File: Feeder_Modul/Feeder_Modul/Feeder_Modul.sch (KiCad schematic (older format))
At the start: 101 parts, among them J1 Conn_02x01, J101 Conn_02x01, J102 Conn_01x06_Male, J103 Conn_02x01, J104 Conn_02x01, J105 Conn_02x01, J106 WE_629104190121, J107 Conn_02x07_Odd_Even, J108 Conn_02x01, J109 Conn_02x01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

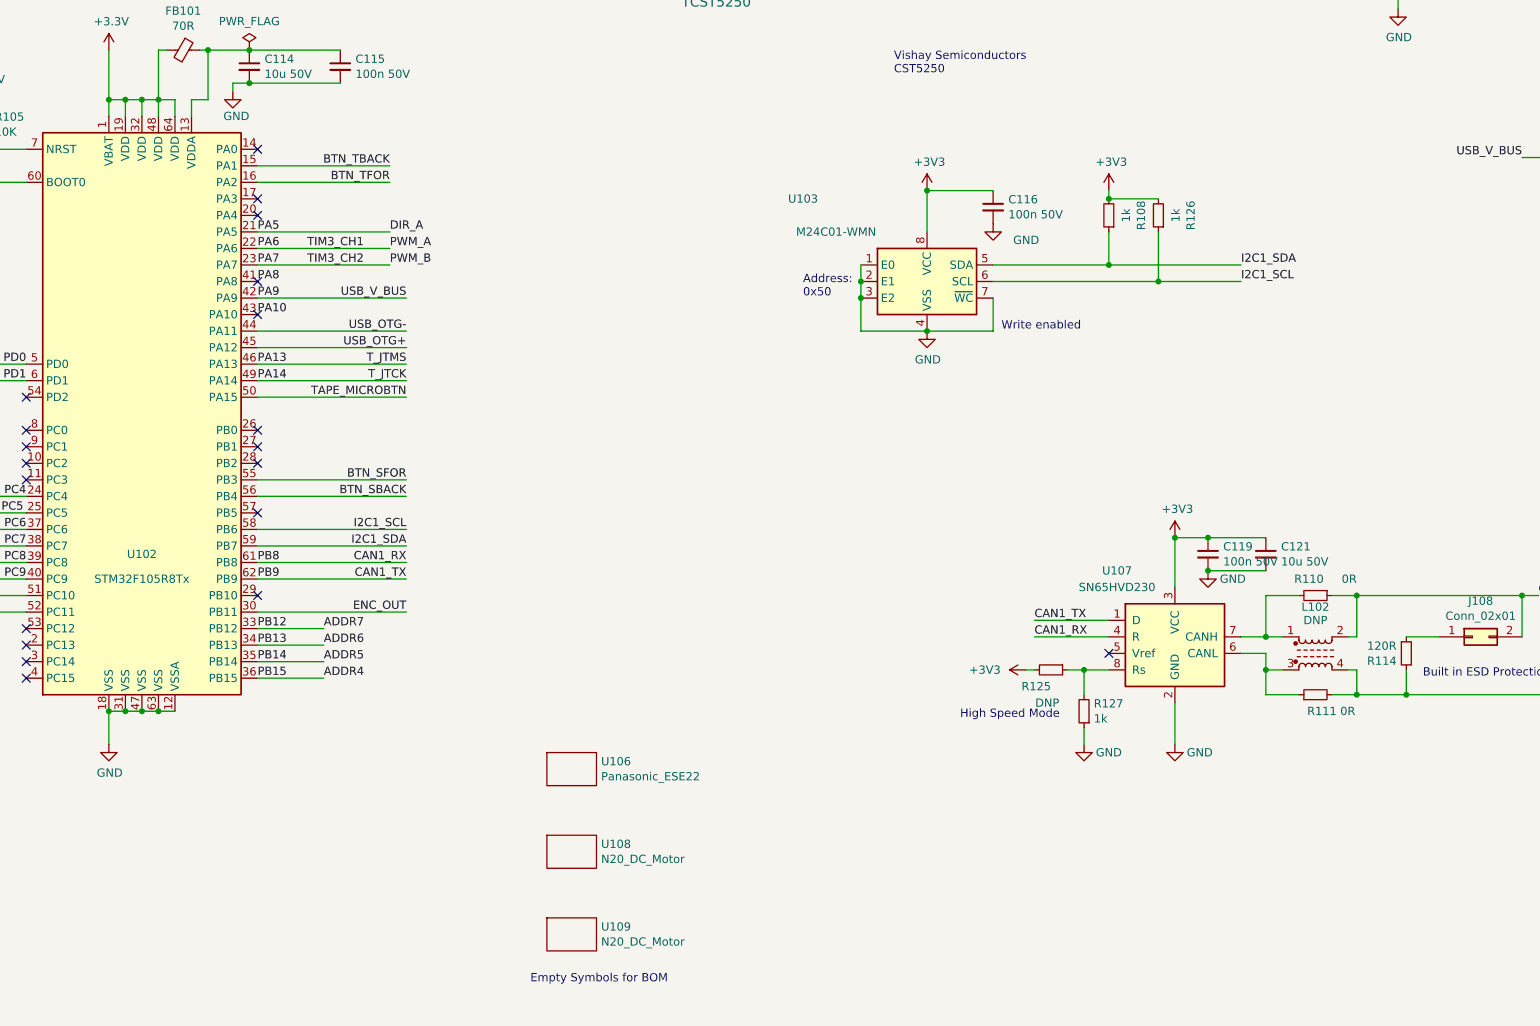
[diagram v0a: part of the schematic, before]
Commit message: ESD Protection für Feeder Modul USB hinzugefügt, Status LED für Controller Modul hinzugefügt
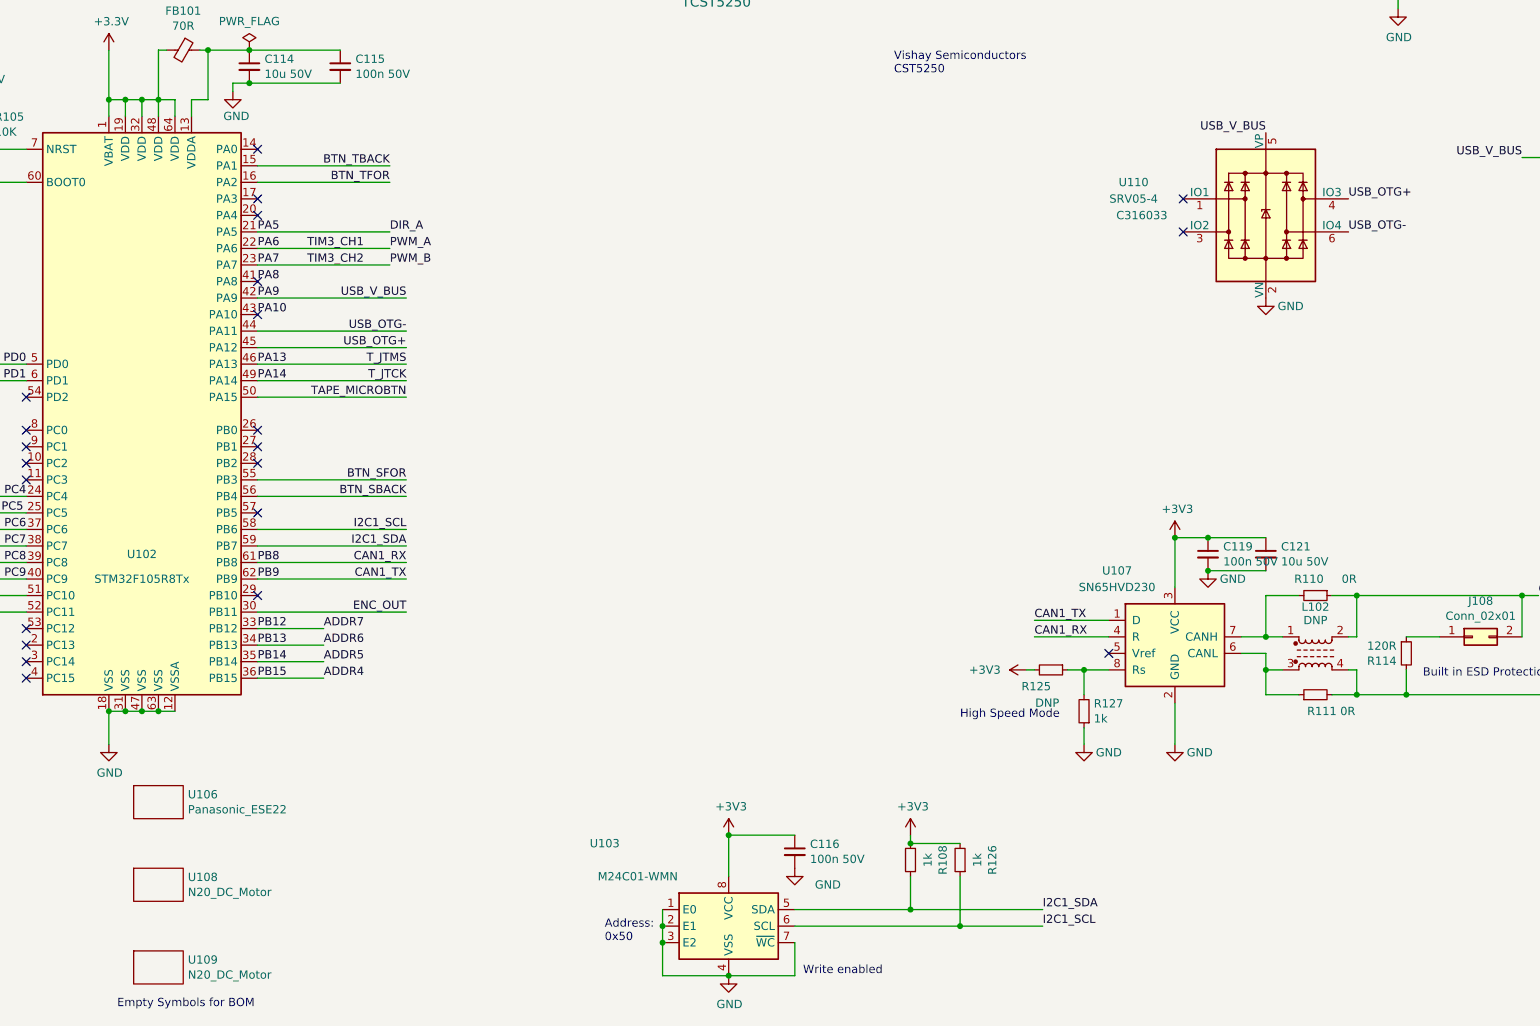
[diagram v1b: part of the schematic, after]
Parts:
- added U110: SRV05-4, Package_TO_SOT_SMD:SOT-23-6, symbol Power_Protection:SRV05-4
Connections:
- net +5V: now also U110.5 (VP)
- net GND: now also U110.2 (VN)
- net USB_OTG+: now also U110.4 (IO3)
- net USB_OTG-: now also U110.6 (IO4)
- no-connect marks 21 -> 23
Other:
- moved on the sheet: C116, R108, R126, U103, U106, U108, U109
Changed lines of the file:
@@
 L Memory_EEPROM:M24C01-WMN U103
 U 1 1 6025867E
-P 9300 6650
-F 0 "U103" H 8550 7150 50  0000 C CNN
-F 1 "M24C01-WMN" H 8750 6950 50  0000 C CNN
-F 2 "Package_SO:SOIC-8_3.9x4.9mm_P1.27mm" H 9300 7000 50  0001 C CNN
-F 3 "http://www.st.com/content/ccc/resource/technical/document/datasheet/b0/d8/50/40/5a/85/49/6f/DM00071904.pdf/files/DM00071904.pdf/jcr:content/translations/en.DM00071904.pdf" H 9350 6150 50  0001 C CNN
-F 4 "C7996" H 9300 6650 50  0001 C CNN "LCSC"
-	1    9300 6650
+P 8100 10550
+F 0 "U103" H 7350 11050 50  0000 C CNN
+F 1 "M24C01-WMN" H 7550 10850 50  0000 C CNN
+F 2 "Package_SO:SOIC-8_3.9x4.9mm_P1.27mm" H 8100 10900 50  0001 C CNN
+F 3 "http://www.st.com/content/ccc/resource/technical/document/datasheet/b0/d8/50/40/5a/85/49/6f/DM00071904.pdf/files/DM00071904.pdf/jcr:content/translations/en.DM00071904.pdf" H 8150 10050 50  0001 C CNN
+F 4 "C7996" H 8100 10550 50  0001 C CNN "LCSC"
+	1    8100 10550
 	1    0    0    -1
 $EndComp
@@
 L power:GND #PWR0154
 U 1 1 60259B94
-P 9300 6950
-F 0 "#PWR0154" H 9300 6700 50  0001 C CNN
-F 1 "GND" H 9305 6777 50  0000 C CNN
-F 2 "" H 9300 6950 50  0001 C CNN
-F 3 "" H 9300 6950 50  0001 C CNN
-	1    9300 6950
-	1    0    0    -1
-$EndComp
-Wire Wire Line
-	9300 6100 9300 6350
+P 8100 10850
+F 0 "#PWR0154" H 8100 10600 50  0001 C CNN
+F 1 "GND" H 8105 10677 50  0000 C CNN
+F 2 "" H 8100 10850 50  0001 C CNN
+F 3 "" H 8100 10850 50  0001 C CNN
+	1    8100 10850
+	1    0    0    -1
+$EndComp
+Wire Wire Line
+	8100 10000 8100 10250
 $Comp
 L Device:C_Small C?
 U 1 1 602778D6
-P 9700 6200
+P 8500 10100
 AR Path="/5FDD0F66/602778D6" Ref="C?"  Part="1"
 AR Path="/602778D6" Ref="C116"  Part="1"
-F 0 "C116" H 9792 6246 50  0000 L CNN
-F 1 "100n 50V" H 9792 6155 50  0000 L CNN
-F 2 "Capacitor_SMD:C_0603_1608Metric" H 9700 6200 50  0001 C CNN
-F 3 "~" H 9700 6200 50  0001 C CNN
-F 4 "C282519" H 9700 6200 50  0001 C CNN "LCSC"
-	1    9700 6200
-	1    0    0    -1
-$EndComp
-Wire Wire Line
-	9700 6100 9300 6100
-Connection ~ 9300 6100
+F 0 "C116" H 8592 10146 50  0000 L CNN
+F 1 "100n 50V" H 8592 10055 50  0000 L CNN
+F 2 "Capacitor_SMD:C_0603_1608Metric" H 8500 10100 50  0001 C CNN
+F 3 "~" H 8500 10100 50  0001 C CNN
+F 4 "C282519" H 8500 10100 50  0001 C CNN "LCSC"
+	1    8500 10100
+	1    0    0    -1
+$EndComp
+Wire Wire Line
+	8500 10000 8100 10000
+Connection ~ 8100 10000
 $Comp
 L power:GND #PWR0155
 U 1 1 60292533
-P 9700 6300
-F 0 "#PWR0155" H 9700 6050 50  0001 C CNN
-F 1 "GND" H 9900 6200 50  0000 C CNN
-F 2 "" H 9700 6300 50  0001 C CNN
-F 3 "" H 9700 6300 50  0001 C CNN
-	1    9700 6300
-	1    0    0    -1
-$EndComp
-Wire Wire Line
-	9300 6950 8900 6950
-Wire Wire Line
-	8900 6950 8900 6750
-Connection ~ 9300 6950
-Connection ~ 8900 6650
-Wire Wire Line
-	8900 6650 8900 6550
-Connection ~ 8900 6750
-Wire Wire Line
-	8900 6750 8900 6650
-Text Label 11200 6550 0    50   ~ 0
+P 8500 10200
+F 0 "#PWR0155" H 8500 9950 50  0001 C CNN
+F 1 "GND" H 8700 10100 50  0000 C CNN
+F 2 "" H 8500 10200 50  0001 C CNN
+F 3 "" H 8500 10200 50  0001 C CNN
+	1    8500 10200
+	1    0    0    -1
+$EndComp
+Wire Wire Line
+	8100 10850 7700 10850
+Wire Wire Line
+	7700 10850 7700 10650
+Connection ~ 8100 10850
+Connection ~ 7700 10550
+Wire Wire Line
+	7700 10550 7700 10450
+Connection ~ 7700 10650
+Wire Wire Line
+	7700 10650 7700 10550
+Text Label 10000 10450 0    50   ~ 0
 I2C1_SDA
-Text Label 11200 6650 0    50   ~ 0
+Text Label 10000 10550 0    50   ~ 0
 I2C1_SCL
 Wire Wire Line
-	9700 6750 9700 6950
-Wire Wire Line
-	9700 6950 9300 6950
-Text Notes 9750 6950 0    50   ~ 0
+	8500 10650 8500 10850
+Wire Wire Line
+	8500 10850 8100 10850
+Text Notes 8550 10850 0    50   ~ 0
 Write enabled\n
-Text Notes 8550 6750 0    50   ~ 0
+Text Notes 7350 10650 0    50   ~ 0
 Address:\n0x50
 Wire Wire Line
-	11200 6550 10400 6550
-Wire Wire Line
-	9700 6650 10700 6650
+	10000 10450 9200 10450
+Wire Wire Line
+	8500 10550 9500 10550
 Text Label 6150 8250 2    50   ~ 0
 I2C1_SDA
@@
 L Device:R_Small R108
 U 1 1 604EFEEC
-P 10400 6250
-F 0 "R108" V 10204 6250 50  0000 C CNN
-F 1 "1k" V 10295 6250 50  0000 C CNN
-F 2 "Resistor_SMD:R_0603_1608Metric" H 10400 6250 50  0001 C CNN
-F 3 "~" H 10400 6250 50  0001 C CNN
-F 4 "C21190" H 10400 6250 50  0001 C CNN "LCSC"
-	1    10400 6250
+P 9200 10150
+F 0 "R108" V 9004 10150 50  0000 C CNN
+F 1 "1k" V 9095 10150 50  0000 C CNN
+F 2 "Resistor_SMD:R_0603_1608Metric" H 9200 10150 50  0001 C CNN
+F 3 "~" H 9200 10150 50  0001 C CNN
+F 4 "C21190" H 9200 10150 50  0001 C CNN "LCSC"
+	1    9200 10150
 	-1   0    0    1
 $EndComp
 Wire Wire Line
-	10400 6350 10400 6550
-Connection ~ 10400 6550
-Wire Wire Line
-	10400 6550 9700 6550
+	9200 10250 9200 10450
+Connection ~ 9200 10450
+Wire Wire Line
+	9200 10450 8500 10450
 $Comp
 L Device:R_Small R126
 U 1 1 6052A30B
-P 10700 6250
-F 0 "R126" V 10504 6250 50  0000 C CNN
-F 1 "1k" V 10595 6250 50  0000 C CNN
-F 2 "Resistor_SMD:R_0603_1608Metric" H 10700 6250 50  0001 C CNN
-F 3 "~" H 10700 6250 50  0001 C CNN
-F 4 "C21190" H 10700 6250 50  0001 C CNN "LCSC"
-	1    10700 6250
+P 9500 10150
+F 0 "R126" V 9304 10150 50  0000 C CNN
+F 1 "1k" V 9395 10150 50  0000 C CNN
+F 2 "Resistor_SMD:R_0603_1608Metric" H 9500 10150 50  0001 C CNN
+F 3 "~" H 9500 10150 50  0001 C CNN
+F 4 "C21190" H 9500 10150 50  0001 C CNN "LCSC"
+	1    9500 10150
 	-1   0    0    1
 $EndComp
 Wire Wire Line
-	10700 6350 10700 6650
-Connection ~ 10700 6650
-Wire Wire Line
-	10700 6650 11200 6650
+	9500 10250 9500 10550
+Connection ~ 9500 10550
+Wire Wire Line
+	9500 10550 10000 10550
 $Comp
 L power:+3V3 #PWR0153
 U 1 1 6025A23B
-P 9300 6100
-F 0 "#PWR0153" H 9300 5950 50  0001 C CNN
-F 1 "+3V3" H 9315 6273 50  0000 C CNN
-F 2 "" H 9300 6100 50  0001 C CNN
-F 3 "" H 9300 6100 50  0001 C CNN
-	1    9300 6100
+P 8100 10000
+F 0 "#PWR0153" H 8100 9850 50  0001 C CNN
+F 1 "+3V3" H 8115 10173 50  0000 C CNN
+F 2 "" H 8100 10000 50  0001 C CNN
+F 3 "" H 8100 10000 50  0001 C CNN
+	1    8100 10000
 	1    0    0    -1
 $EndComp
@@
 L power:+3V3 #PWR0156
 U 1 1 6055FB3C
-P 10400 6100
-F 0 "#PWR0156" H 10400 5950 50  0001 C CNN
-F 1 "+3V3" H 10415 6273 50  0000 C CNN
-F 2 "" H 10400 6100 50  0001 C CNN
-F 3 "" H 10400 6100 50  0001 C CNN
-	1    10400 6100
-	1    0    0    -1
-$EndComp
-Wire Wire Line
-	10700 6150 10400 6150
-Wire Wire Line
-	10400 6100 10400 6150
-Connection ~ 10400 6150
+P 9200 10000
+F 0 "#PWR0156" H 9200 9850 50  0001 C CNN
+F 1 "+3V3" H 9215 10173 50  0000 C CNN
+F 2 "" H 9200 10000 50  0001 C CNN
+F 3 "" H 9200 10000 50  0001 C CNN
+	1    9200 10000
+	1    0    0    -1
+$EndComp
+Wire Wire Line
+	9500 10050 9200 10050
+Wire Wire Line
+	9200 10000 9200 10050
+Connection ~ 9200 10050
 NoConn ~ 5250 7550
 NoConn ~ 5250 7650
@@
 L PorjectLibrary:Empty U106
 U 1 1 601D655D
-P 7150 9600
-F 0 "U106" H 7328 9646 50  0000 L CNN
-F 1 "Panasonic_ESE22" H 7328 9555 50  0000 L CNN
-F 2 "ProjectFootprints:Empty" H 7150 9600 50  0001 C CNN
-F 3 "" H 7150 9600 50  0001 C CNN
-F 4 "0" H 7150 9600 50  0001 C CNN "LCSC"
-	1    7150 9600
+P 4650 9800
+F 0 "U106" H 4828 9846 50  0000 L CNN
+F 1 "Panasonic_ESE22" H 4828 9755 50  0000 L CNN
+F 2 "ProjectFootprints:Empty" H 4650 9800 50  0001 C CNN
+F 3 "" H 4650 9800 50  0001 C CNN
+F 4 "0" H 4650 9800 50  0001 C CNN "LCSC"
+	1    4650 9800
 	1    0    0    -1
 $EndComp
@@
 L PorjectLibrary:Empty U108
 U 1 1 602321B1
-P 7150 10100
-F 0 "U108" H 7328 10146 50  0000 L CNN
-F 1 "N20_DC_Motor" H 7328 10055 50  0000 L CNN
-F 2 "ProjectFootprints:Empty" H 7150 10100 50  0001 C CNN
-F 3 "" H 7150 10100 50  0001 C CNN
-F 4 "0" H 7150 10100 50  0001 C CNN "LCSC"
-	1    7150 10100
+P 4650 10300
+F 0 "U108" H 4828 10346 50  0000 L CNN
+F 1 "N20_DC_Motor" H 4828 10255 50  0000 L CNN
+F 2 "ProjectFootprints:Empty" H 4650 10300 50  0001 C CNN
+F 3 "" H 4650 10300 50  0001 C CNN
+F 4 "0" H 4650 10300 50  0001 C CNN "LCSC"
+	1    4650 10300
 	1    0    0    -1
 $EndComp
@@
 L PorjectLibrary:Empty U109
 U 1 1 60254EDC
-P 7150 10600
-F 0 "U109" H 7328 10646 50  0000 L CNN
-F 1 "N20_DC_Motor" H 7328 10555 50  0000 L CNN
-F 2 "ProjectFootprints:Empty" H 7150 10600 50  0001 C CNN
-F 3 "" H 7150 10600 50  0001 C CNN
-F 4 "0" H 7150 10600 50  0001 C CNN "LCSC"
-	1    7150 10600
-	1    0    0    -1
-$EndComp
-Text Notes 6900 10900 0    50   ~ 0
+P 4650 10800
+F 0 "U109" H 4828 10846 50  0000 L CNN
+F 1 "N20_DC_Motor" H 4828 10755 50  0000 L CNN
+F 2 "ProjectFootprints:Empty" H 4650 10800 50  0001 C CNN
+F 3 "" H 4650 10800 50  0001 C CNN
+F 4 "0" H 4650 10800 50  0001 C CNN "LCSC"
+	1    4650 10800
+	1    0    0    -1
+$EndComp
+Text Notes 4400 11050 0    50   ~ 0
 Empty Symbols for BOM
 Text Label 15250 8800 2    50   ~ 0
@@
 Wire Wire Line
 	14050 8900 14400 8900
+$Comp
+L Power_Protection:SRV05-4 U110
+U 1 1 60371E49
+P 11350 6250
+F 0 "U110" H 10550 6450 50  0000 C CNN
+F 1 "SRV05-4" H 10550 6350 50  0000 C CNN
+F 2 "Package_TO_SOT_SMD:SOT-23-6" H 12050 5800 50  0001 C CNN
+F 3 "http://www.onsemi.com/pub/Collateral/SRV05-4-D.PDF" H 11350 6250 50  0001 C CNN
+F 4 "C316033" H 10600 6250 50  0000 C CNN "LCSC"
+	1    11350 6250
+	1    0    0    -1
+$EndComp
+$Comp
+L power:GND #PWR?
+U 1 1 60371E4F
+P 11350 6750
+AR Path="/5FDD0F66/60371E4F" Ref="#PWR?"  Part="1"
+AR Path="/60371E4F" Ref="#PWR0135"  Part="1"
+F 0 "#PWR0135" H 11350 6500 50  0001 C CNN
+F 1 "GND" H 11500 6700 50  0000 C CNN
+F 2 "" H 11350 6750 50  0001 C CNN
+F 3 "" H 11350 6750 50  0001 C CNN
+	1    11350 6750
+	1    0    0    -1
+$EndComp
+Text Label 11350 5750 2    50   ~ 0
+USB_V_BUS
+Text Label 11850 6150 0    50   ~ 0
+USB_OTG+
+Text Label 11850 6350 0    50   ~ 0
+USB_OTG-
+NoConn ~ 10850 6150
+NoConn ~ 10850 6350
 $EndSCHEMATC

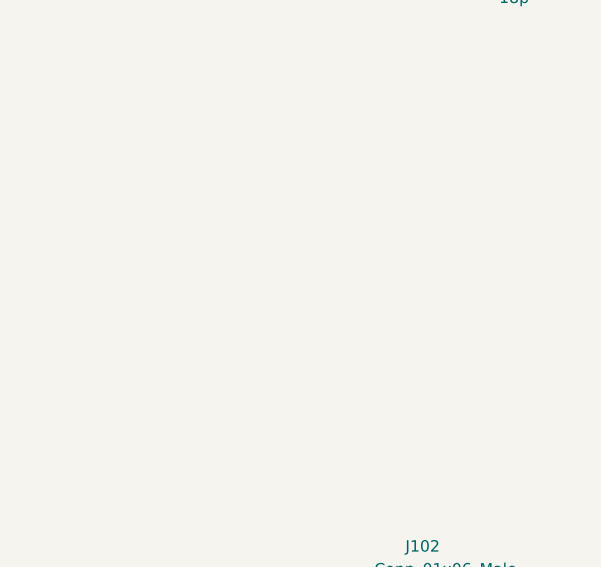
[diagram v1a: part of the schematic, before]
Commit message: Fiducials auf allen Boards hinzugefügt
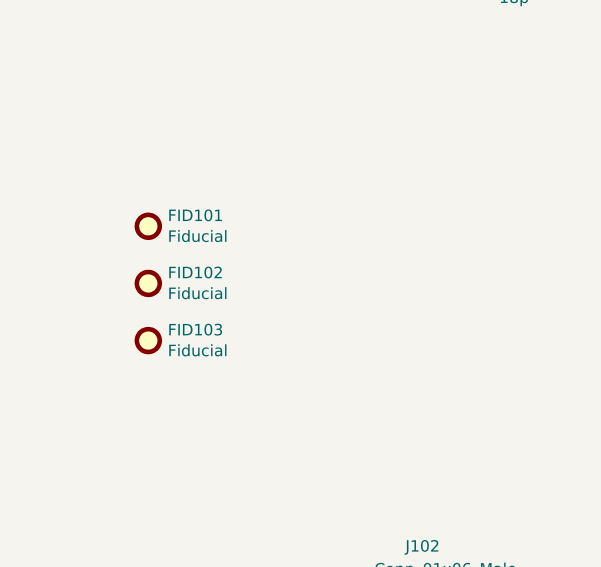
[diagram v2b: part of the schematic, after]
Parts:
- added FID101, FID102, FID103: Fiducial, Fiducial:Fiducial_1mm_Mask2mm, symbol Mechanical:Fiducial
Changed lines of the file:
@@
 NoConn ~ 10850 6150
 NoConn ~ 10850 6350
+$Comp
+L Mechanical:Fiducial FID101
+U 1 1 6025399D
+P 1000 8500
+F 0 "FID101" H 1085 8546 50  0000 L CNN
+F 1 "Fiducial" H 1085 8455 50  0000 L CNN
+F 2 "Fiducial:Fiducial_1mm_Mask2mm" H 1000 8500 50  0001 C CNN
+F 3 "~" H 1000 8500 50  0001 C CNN
+	1    1000 8500
+	1    0    0    -1
+$EndComp
+$Comp
+L Mechanical:Fiducial FID102
+U 1 1 60254D5A
+P 1000 8750
+F 0 "FID102" H 1085 8796 50  0000 L CNN
+F 1 "Fiducial" H 1085 8705 50  0000 L CNN
+F 2 "Fiducial:Fiducial_1mm_Mask2mm" H 1000 8750 50  0001 C CNN
+F 3 "~" H 1000 8750 50  0001 C CNN
+	1    1000 8750
+	1    0    0    -1
+$EndComp
+$Comp
+L Mechanical:Fiducial FID103
+U 1 1 602552E6
+P 1000 9000
+F 0 "FID103" H 1085 9046 50  0000 L CNN
+F 1 "Fiducial" H 1085 8955 50  0000 L CNN
+F 2 "Fiducial:Fiducial_1mm_Mask2mm" H 1000 9000 50  0001 C CNN
+F 3 "~" H 1000 9000 50  0001 C CNN
+	1    1000 9000
+	1    0    0    -1
+$EndComp
 $EndSCHEMATC

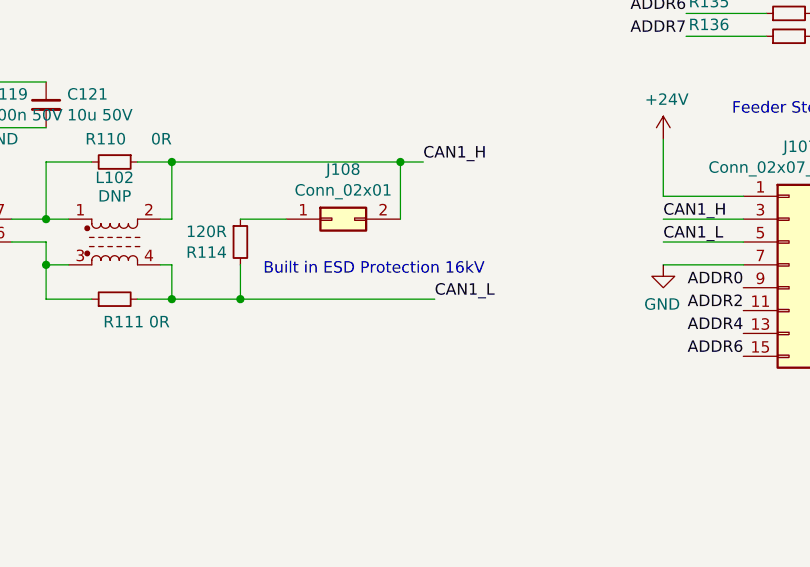
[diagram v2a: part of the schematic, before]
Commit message: ESD Protection überarbeitet, aber noch nicht fertig
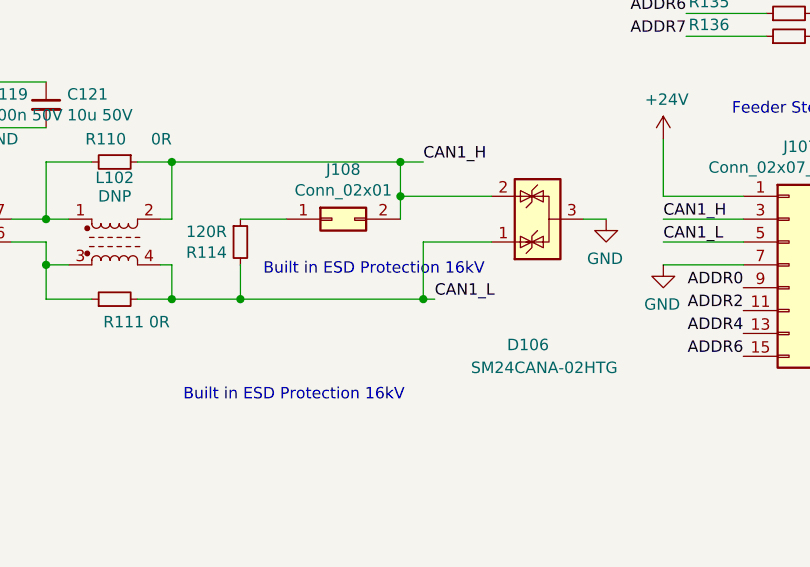
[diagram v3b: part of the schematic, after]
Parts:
- added D106: SM24CANA-02HTG, Package_TO_SOT_SMD:SOT-23, symbol Power_Protection:NUP2105L
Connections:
- net CAN1_H: now also D106.2 (K)
- net CAN1_L: now also D106.1 (K)
- net GND: now also D106.3 (A)
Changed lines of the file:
@@
 Connection ~ 11900 8550
 Wire Wire Line
-	13050 9150 12200 9150
+	13050 9150 13000 9150
 Connection ~ 11900 9150
 Wire Wire Line
-	12900 8800 12900 8550
+	12900 8800 12900 8700
 Connection ~ 12900 8550
 Wire Wire Line
@@
 	1    0    0    -1
 $EndComp
+Text Notes 11950 9600 0    50   ~ 0
+Built in ESD Protection 16kV
+$Comp
+L Power_Protection:NUP2105L D106
+U 1 1 6054232A
+P 13500 8800
+F 0 "D106" V 12950 8750 50  0000 L CNN
+F 1 "SM24CANA-02HTG" V 12850 8450 50  0000 L CNN
+F 2 "Package_TO_SOT_SMD:SOT-23" H 13725 8750 50  0001 L CNN
+F 3 "http://www.onsemi.com/pub_link/Collateral/NUP2105L-D.PDF" H 13625 8925 50  0001 C CNN
+F 4 "C151236" H 13500 8800 50  0001 C CNN "LCSC"
+	1    13500 8800
+	0    -1   -1   0
+$EndComp
+Wire Wire Line
+	13300 8900 13000 8900
+Wire Wire Line
+	13000 8900 13000 9150
+Connection ~ 13000 9150
+Wire Wire Line
+	13000 9150 12200 9150
+Wire Wire Line
+	13300 8700 12900 8700
+Connection ~ 12900 8700
+Wire Wire Line
+	12900 8700 12900 8550
+$Comp
+L power:GND #PWR0138
+U 1 1 605AEC06
+P 13800 8800
+F 0 "#PWR0138" H 13800 8550 50  0001 C CNN
+F 1 "GND" H 13805 8627 50  0000 C CNN
+F 2 "" H 13800 8800 50  0001 C CNN
+F 3 "" H 13800 8800 50  0001 C CNN
+	1    13800 8800
+	-1   0    0    -1
+$EndComp
+Wire Wire Line
+	13800 8800 13700 8800
 $EndSCHEMATC
